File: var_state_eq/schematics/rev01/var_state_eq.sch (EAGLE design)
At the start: 69 parts, among them IC1 TL084P, IC2 TL084P, IC3 TL084P, J1 IN, J2 OUT

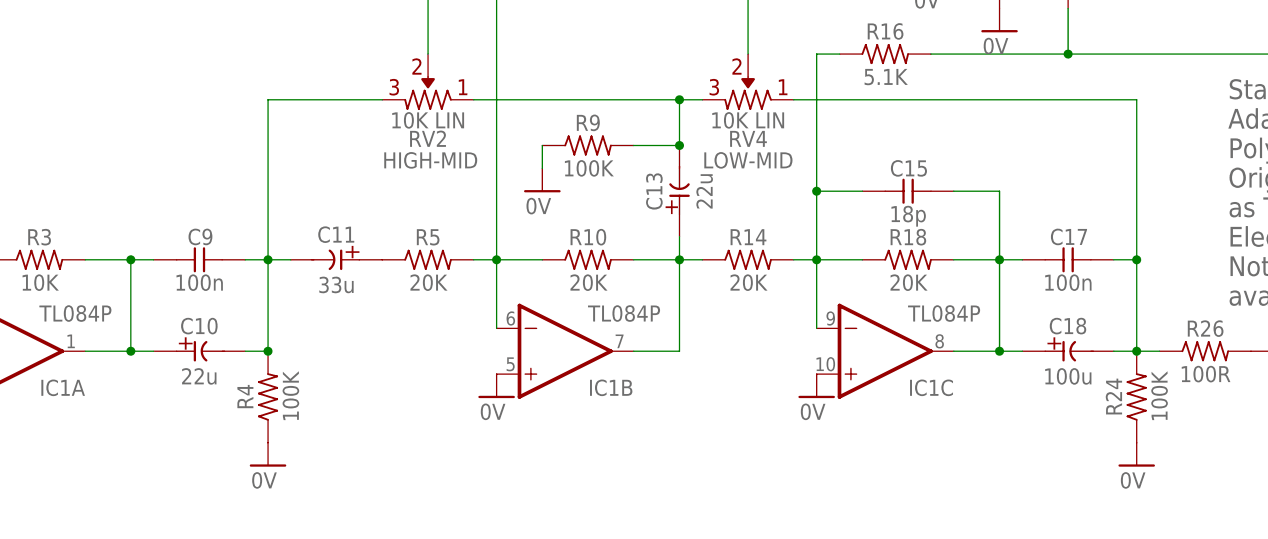
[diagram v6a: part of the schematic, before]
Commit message: Updated cap values
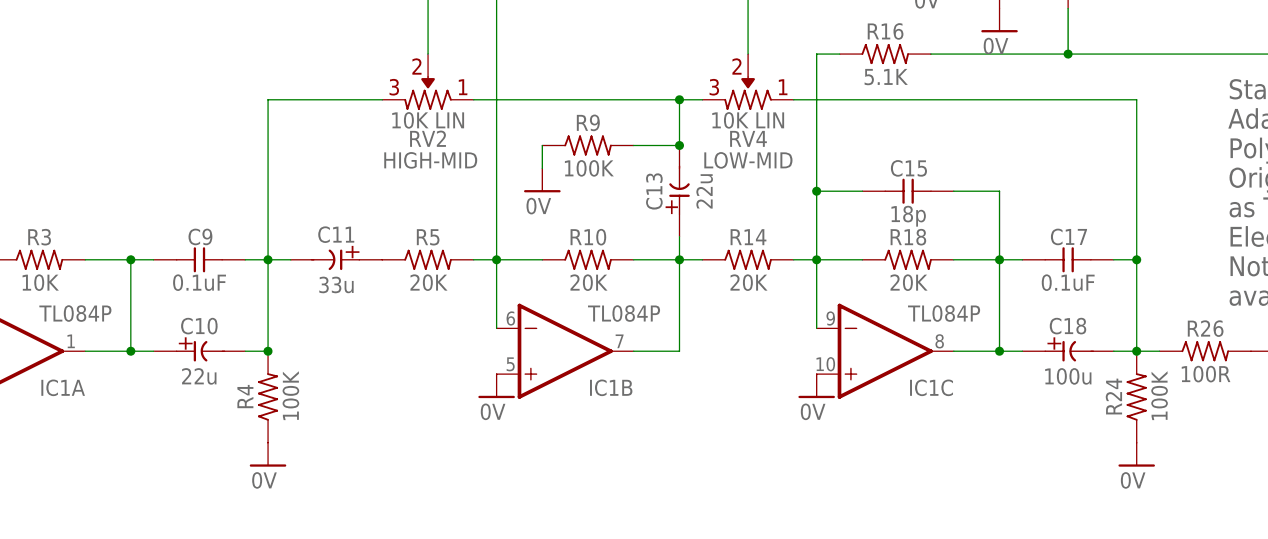
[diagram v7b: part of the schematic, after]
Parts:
- C17, C9: value 100n -> 0.1uF
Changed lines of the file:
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@@
 <part name="R3" library="_common" deviceset="R" device="" value="10K"/>
 <part name="C10" library="_common" deviceset="CE-US" device="E2-5" value="22u"/>
-<part name="C9" library="_common" deviceset="CC-US" device="025-024X044" value="100n"/>
+<part name="C9" library="_common" deviceset="CC-US" device="025-024X044" value="0.1uF"/>
 <part name="R4" library="_common" deviceset="R" device="" value="100K"/>
 <part name="C6" library="_common" deviceset="CC-US" device="025-024X044" value="18p"/>
@@
 <part name="R18" library="_common" deviceset="R" device="" value="20K"/>
 <part name="C15" library="_common" deviceset="CC-US" device="025-024X044" value="18p"/>
-<part name="C17" library="_common" deviceset="CC-US" device="025-024X044" value="100n"/>
+<part name="C17" library="_common" deviceset="CC-US" device="025-024X044" value="0.1uF"/>
 <part name="C18" library="_common" deviceset="CE-US" device="E5-8.5" value="100u"/>
 <part name="R26" library="_common" deviceset="R" device="" value="100R"/>
